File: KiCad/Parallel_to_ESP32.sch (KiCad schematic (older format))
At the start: 21 parts, among them J1 DB25_Male, J2 Micro_SD_Card_Socket, J3 Conn_01x02, J4 Conn_01x02, U1 ESP32-DEVKIT-V1, U2 SN74CB3T16210

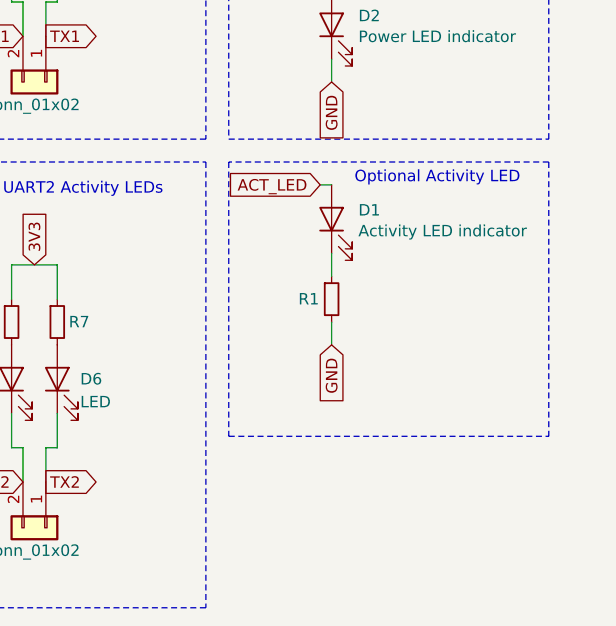
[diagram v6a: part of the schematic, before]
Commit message: fixed activity LED circuit using a PNP-transistor
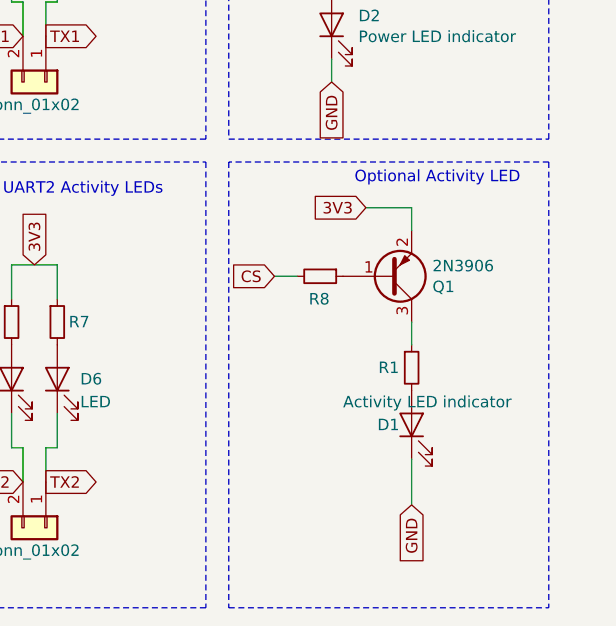
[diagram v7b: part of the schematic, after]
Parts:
- added Q1: 2N3906, Package_TO_SOT_SMD:SOT-23, symbol Transistor_BJT:BC857
- added R8: 1k, Resistor_SMD:R_0603_1608Metric_Pad1.05x0.95mm_HandSolder, symbol Device:R_Small
- R1: footprint Resistor_SMD:R_1206_3216Metric_Pad1.42x1.75mm_HandSolder -> Resistor_SMD:R_0805_2012Metric_Pad1.15x1.40mm_HandSolder
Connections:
- net +3V3: now also Q1.2 (E)
- net CS: now also R8.2
- net GND: now also D1.1 (K); no longer R1.2
- net at R1.1: now also Q1.3 (C); no longer D1.1 (K)
- net ACT_LED: no longer names the net of D1.2 (A)
- net ACT_LED: now also R1.2
- new net: Q1.1 (B), R8.1
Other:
- moved on the sheet: D1, R1
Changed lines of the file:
@@
 CD
-Wire Notes Line
-	9650 5400 11050 5400
 Wire Notes Line
 	11050 4200 9650 4200
@@
 Text GLabel 4700 4100 0    50   Output ~ 0
 CS
-Text GLabel 10050 4300 0    50   Input ~ 0
-ACT_LED
-Wire Notes Line
-	11050 4200 11050 5400
-Wire Notes Line
-	9650 4200 9650 5400
 $Comp
 L Device:C_Small C1
@@
 NoConn ~ 5900 3500
 NoConn ~ 5900 3600
-Wire Wire Line
-	10050 4300 10100 4300
 Text GLabel 4700 3500 0    50   Input ~ 0
 RX1
@@
 Wire Wire Line
 	10100 3850 10100 3750
-Text GLabel 10100 5000 3    50   Input ~ 0
-GND
-Wire Wire Line
-	10100 4900 10100 5000
-Wire Wire Line
-	10100 4600 10100 4700
+Text GLabel 10450 5700 3    50   Input ~ 0
+GND
 $Comp
 L Device:LED D1
 U 1 1 5EBA7223
-P 10100 4450
-F 0 "D1" V 10139 4333 50  0000 R CNN
-F 1 "Activity LED indicator" V 10048 4333 50  0000 R CNN
-F 2 "LED_THT:LED_D3.0mm" H 10100 4450 50  0001 C CNN
-F 3 "~" H 10100 4450 50  0001 C CNN
-	1    10100 4450
+P 10450 5350
+F 0 "D1" V 10450 5500 50  0000 R CNN
+F 1 "Activity LED indicator" V 10550 5650 50  0000 R CNN
+F 2 "LED_THT:LED_D3.0mm" H 10450 5350 50  0001 C CNN
+F 3 "~" H 10450 5350 50  0001 C CNN
+	1    10450 5350
 	0    -1   -1   0
 $EndComp
@@
 L Device:R_Small R1
 U 1 1 5EB9CA00
-P 10100 4800
-F 0 "R1" H 10000 4800 50  0000 C CNN
-F 1 "150" H 10250 4800 50  0001 C CNN
-F 2 "Resistor_SMD:R_1206_3216Metric_Pad1.42x1.75mm_HandSolder" H 10100 4800 50  0001 C CNN
-F 3 "~" H 10100 4800 50  0001 C CNN
-	1    10100 4800
-	1    0    0    -1
-$EndComp
+P 10450 5100
+F 0 "R1" H 10350 5100 50  0000 C CNN
+F 1 "150" H 10600 5100 50  0001 C CNN
+F 2 "Resistor_SMD:R_0805_2012Metric_Pad1.15x1.40mm_HandSolder" H 10450 5100 50  0001 C CNN
+F 3 "~" H 10450 5100 50  0001 C CNN
+	1    10450 5100
+	1    0    0    -1
+$EndComp
+Text GLabel 9850 4700 0    50   Input ~ 0
+CS
+$Comp
+L Transistor_BJT:BC857 Q1
+U 1 1 64612433
+P 10350 4700
+F 0 "Q1" H 10541 4746 50  0000 L CNN
+F 1 "2N3906" H 10541 4655 50  0000 L CNN
+F 2 "Package_TO_SOT_SMD:SOT-23" H 10550 4625 50  0001 L CIN
+F 3 "" H 10350 4700 50  0001 L CNN
+	1    10350 4700
+	1    0    0    1
+$EndComp
+Text GLabel 10250 4400 0    50   Input ~ 0
+3V3
+Wire Wire Line
+	10250 4400 10450 4400
+Wire Wire Line
+	10450 4400 10450 4500
+$Comp
+L Device:R_Small R8
+U 1 1 6462427B
+P 10050 4700
+F 0 "R8" V 10150 4650 50  0000 L CNN
+F 1 "1k" H 10100 4700 50  0001 L CNN
+F 2 "Resistor_SMD:R_0603_1608Metric_Pad1.05x0.95mm_HandSolder" H 10050 4700 50  0001 C CNN
+F 3 "~" H 10050 4700 50  0001 C CNN
+	1    10050 4700
+	0    1    1    0
+$EndComp
+Wire Wire Line
+	9850 4700 9950 4700
+Wire Wire Line
+	10450 4900 10450 5000
+Wire Wire Line
+	10450 5500 10450 5700
+Wire Notes Line
+	9650 6150 11050 6150
+Wire Notes Line
+	11050 4200 11050 6150
+Wire Notes Line
+	9650 4200 9650 6150
 $EndSCHEMATC

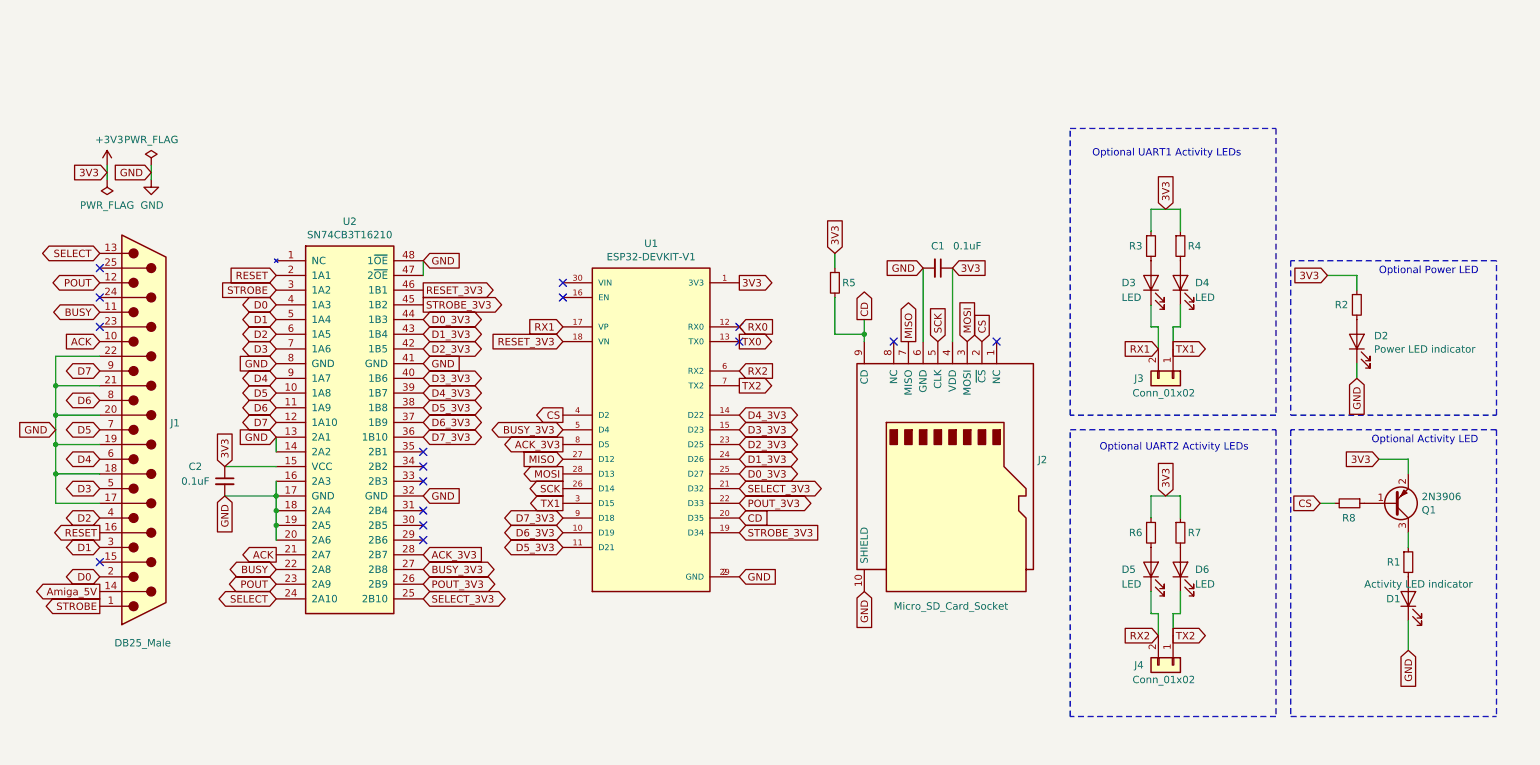
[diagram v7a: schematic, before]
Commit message: Re-assignment of some pins and simplified Activity LED circuit
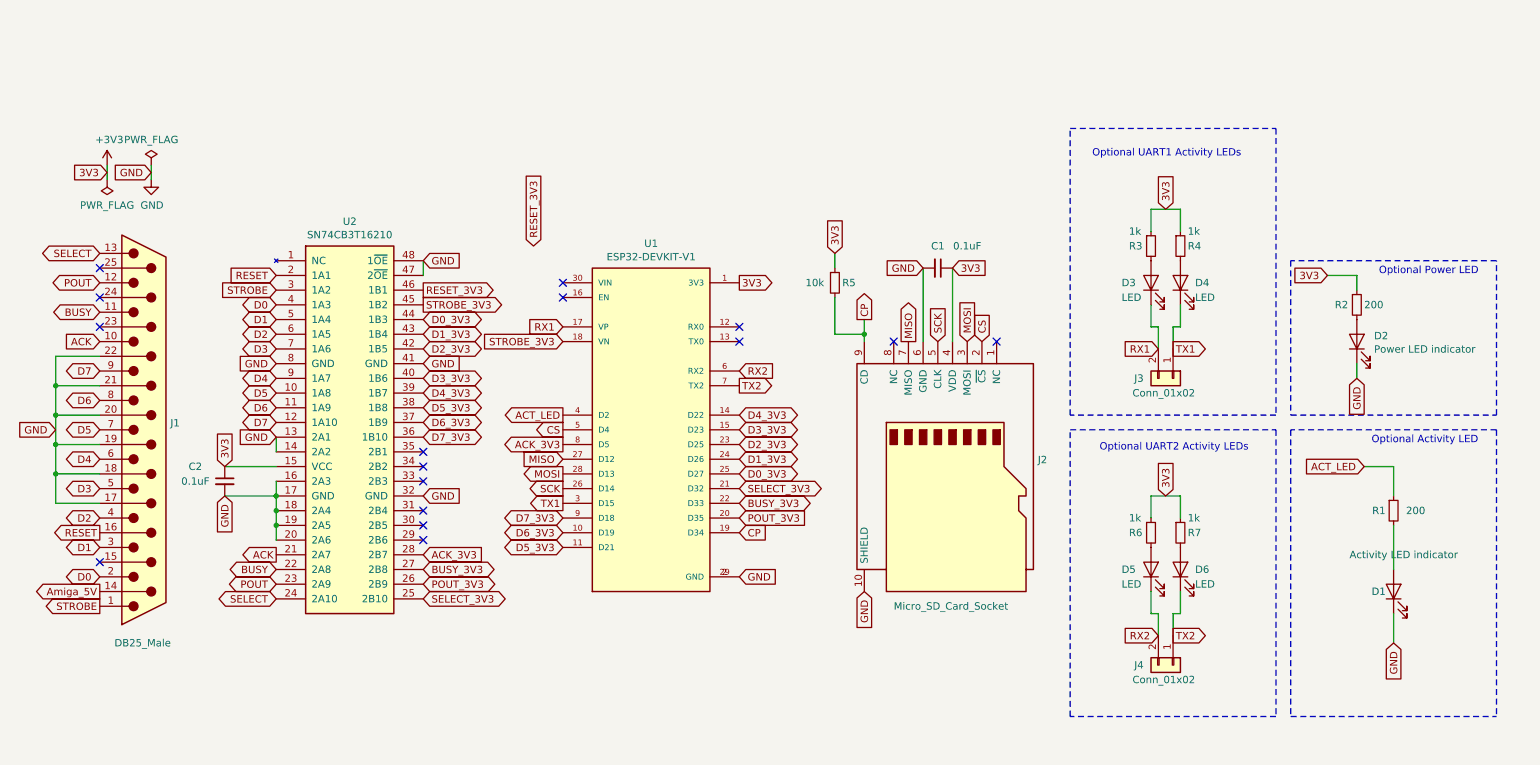
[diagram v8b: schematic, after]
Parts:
- removed Q1: 2N3906, Package_TO_SOT_SMD:SOT-23, symbol Transistor_BJT:BC857
- removed R8: 1k, Resistor_SMD:R_0603_1608Metric_Pad1.05x0.95mm_HandSolder, symbol Device:R_Small
- R1, R2: value 150 -> 200
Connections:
- net BUSY_3V3: now also U1.22 (D33); no longer U1.5 (D4)
- net CS: now also U1.5 (D4); no longer U1.4 (D2)
- net POUT_3V3: now also U1.20 (D35); no longer U1.22 (D33)
- net RESET_3V3: no longer U1.18 (VN)
- net STROBE_3V3: now also U1.18 (VN); no longer U1.19 (D34)
- net ACT_LED: now reaches R1.1
- net ACT_LED: now also U1.4 (D2)
- net CD renamed CP
- net CP: now also U1.19 (D34); no longer U1.20 (D35)
- net RX0: no longer names the net of U1.12 (RX0)
- net TX0: no longer names the net of U1.13 (TX0)
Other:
- moved on the sheet: D1, R1
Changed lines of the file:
@@
 P 10100 3350
 F 0 "R2" H 9950 3350 50  0000 L CNN
-F 1 "150" H 10150 3350 50  0001 L CNN
+F 1 "200" H 10150 3350 50  0000 L CNN
 F 2 "Resistor_SMD:R_0805_2012Metric_Pad1.15x1.40mm_HandSolder" H 10100 3350 50  0001 C CNN
 F 3 "~" H 10100 3350 50  0001 C CNN
@@
 CS
 Text GLabel 6750 3450 1    50   Output ~ 0
-CD
+CP
 Wire Notes Line
 	11050 4200 9650 4200
-Text GLabel 5900 4800 2    50   Input ~ 0
-CD
-Text GLabel 4700 4100 0    50   Output ~ 0
-CS
+Text GLabel 5900 4900 2    50   Input ~ 0
+CP
 $Comp
 L Device:C_Small C1
@@
 Text GLabel 4700 4300 0    50   Output ~ 0
 ACK_3V3
-Text GLabel 4700 4200 0    50   BiDi ~ 0
-BUSY_3V3
-Text GLabel 5900 4700 2    50   BiDi ~ 0
+Text GLabel 5900 4800 2    50   Input ~ 0
 POUT_3V3
 Text GLabel 5900 4600 2    50   BiDi ~ 0
@@
 D7_3V3
 NoConn ~ 4700 3300
-Text GLabel 5900 3500 2    50   Input ~ 0
-RX0
-Text GLabel 5900 3600 2    50   Output ~ 0
-TX0
-Text GLabel 5900 4900 2    50   Input ~ 0
+Text GLabel 4700 3600 0    50   Input ~ 0
 STROBE_3V3
-Text GLabel 4700 3600 0    50   Input ~ 0
+Text GLabel 4500 2950 1    50   Input ~ 0
 RESET_3V3
 Text GLabel 3750 3050 2    50   Input ~ 0
@@
 P 8700 2950
 F 0 "R3" H 8550 2950 50  0000 L CNN
-F 1 "1k" H 8750 2950 50  0001 L CNN
+F 1 "1k" H 8550 3050 50  0000 L CNN
 F 2 "Resistor_SMD:R_0603_1608Metric_Pad1.05x0.95mm_HandSolder" H 8700 2950 50  0001 C CNN
 F 3 "~" H 8700 2950 50  0001 C CNN
@@
 P 8900 2950
 F 0 "R4" H 8950 2950 50  0000 L CNN
-F 1 "1k" H 8950 2950 50  0001 L CNN
+F 1 "1k" H 8950 3050 50  0000 L CNN
 F 2 "Resistor_SMD:R_0603_1608Metric_Pad1.05x0.95mm_HandSolder" H 8900 2950 50  0001 C CNN
 F 3 "~" H 8900 2950 50  0001 C CNN
@@
 P 6550 3200
 F 0 "R5" H 6600 3200 50  0000 L CNN
-F 1 "10k" H 6600 3200 50  0001 L CNN
+F 1 "10k" H 6350 3200 50  0000 L CNN
 F 2 "Resistor_SMD:R_0603_1608Metric_Pad1.05x0.95mm_HandSolder" H 6550 3200 50  0001 C CNN
 F 3 "~" H 6550 3200 50  0001 C CNN
@@
 P 8700 4900
 F 0 "R6" H 8550 4900 50  0000 L CNN
-F 1 "1k" H 8750 4900 50  0001 L CNN
+F 1 "1k" H 8550 5000 50  0000 L CNN
 F 2 "Resistor_SMD:R_0603_1608Metric_Pad1.05x0.95mm_HandSolder" H 8700 4900 50  0001 C CNN
 F 3 "~" H 8700 4900 50  0001 C CNN
@@
 P 8900 4900
 F 0 "R7" H 8950 4900 50  0000 L CNN
-F 1 "1k" H 8950 4900 50  0001 L CNN
+F 1 "1k" H 8950 5000 50  0000 L CNN
 F 2 "Resistor_SMD:R_0603_1608Metric_Pad1.05x0.95mm_HandSolder" H 8900 4900 50  0001 C CNN
 F 3 "~" H 8900 4900 50  0001 C CNN
@@
 Wire Wire Line
 	10100 3850 10100 3750
-Text GLabel 10450 5700 3    50   Input ~ 0
+Text GLabel 10350 5650 3    50   Input ~ 0
 GND
 $Comp
 L Device:LED D1
 U 1 1 5EBA7223
-P 10450 5350
-F 0 "D1" V 10450 5500 50  0000 R CNN
-F 1 "Activity LED indicator" V 10550 5650 50  0000 R CNN
-F 2 "LED_THT:LED_D3.0mm" H 10450 5350 50  0001 C CNN
-F 3 "~" H 10450 5350 50  0001 C CNN
-	1    10450 5350
+P 10350 5300
+F 0 "D1" V 10350 5450 50  0000 R CNN
+F 1 "Activity LED indicator" V 10600 5600 50  0000 R CNN
+F 2 "LED_THT:LED_D3.0mm" H 10350 5300 50  0001 C CNN
+F 3 "~" H 10350 5300 50  0001 C CNN
+	1    10350 5300
 	0    -1   -1   0
 $EndComp
@@
 L Device:R_Small R1
 U 1 1 5EB9CA00
-P 10450 5100
-F 0 "R1" H 10350 5100 50  0000 C CNN
-F 1 "150" H 10600 5100 50  0001 C CNN
-F 2 "Resistor_SMD:R_0805_2012Metric_Pad1.15x1.40mm_HandSolder" H 10450 5100 50  0001 C CNN
-F 3 "~" H 10450 5100 50  0001 C CNN
-	1    10450 5100
-	1    0    0    -1
-$EndComp
-Text GLabel 9850 4700 0    50   Input ~ 0
+P 10350 4750
+F 0 "R1" H 10250 4750 50  0000 C CNN
+F 1 "200" H 10500 4750 50  0000 C CNN
+F 2 "Resistor_SMD:R_0805_2012Metric_Pad1.15x1.40mm_HandSolder" H 10350 4750 50  0001 C CNN
+F 3 "~" H 10350 4750 50  0001 C CNN
+	1    10350 4750
+	1    0    0    -1
+$EndComp
+Text GLabel 10150 4450 0    50   Input ~ 0
+ACT_LED
+Wire Wire Line
+	10150 4450 10350 4450
+Wire Wire Line
+	10350 5450 10350 5650
+Wire Notes Line
+	9650 6150 11050 6150
+Wire Notes Line
+	11050 4200 11050 6150
+Wire Notes Line
+	9650 4200 9650 6150
+Text GLabel 5900 4700 2    50   BiDi ~ 0
+BUSY_3V3
+Text GLabel 4700 4200 0    50   Output ~ 0
 CS
-$Comp
-L Transistor_BJT:BC857 Q1
-U 1 1 64612433
-P 10350 4700
-F 0 "Q1" H 10541 4746 50  0000 L CNN
-F 1 "2N3906" H 10541 4655 50  0000 L CNN
-F 2 "Package_TO_SOT_SMD:SOT-23" H 10550 4625 50  0001 L CIN
-F 3 "" H 10350 4700 50  0001 L CNN
-	1    10350 4700
-	1    0    0    1
-$EndComp
-Text GLabel 10250 4400 0    50   Input ~ 0
-3V3
-Wire Wire Line
-	10250 4400 10450 4400
-Wire Wire Line
-	10450 4400 10450 4500
-$Comp
-L Device:R_Small R8
-U 1 1 6462427B
-P 10050 4700
-F 0 "R8" V 10150 4650 50  0000 L CNN
-F 1 "1k" H 10100 4700 50  0001 L CNN
-F 2 "Resistor_SMD:R_0603_1608Metric_Pad1.05x0.95mm_HandSolder" H 10050 4700 50  0001 C CNN
-F 3 "~" H 10050 4700 50  0001 C CNN
-	1    10050 4700
-	0    1    1    0
-$EndComp
-Wire Wire Line
-	9850 4700 9950 4700
-Wire Wire Line
-	10450 4900 10450 5000
-Wire Wire Line
-	10450 5500 10450 5700
-Wire Notes Line
-	9650 6150 11050 6150
-Wire Notes Line
-	11050 4200 11050 6150
-Wire Notes Line
-	9650 4200 9650 6150
+Wire Wire Line
+	10350 4450 10350 4650
+Wire Wire Line
+	10350 4850 10350 5150
+Text GLabel 4700 4100 0    50   Output ~ 0
+ACT_LED
 $EndSCHEMATC
